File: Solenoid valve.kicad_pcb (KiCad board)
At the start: 2 copper layers, 27.1 x 24.5 mm, 21 parts, among them J2 Conn_01x02, J3 Conn_01x02, J4 Conn_01x02, Q1 S8050, Q2 S8050, U1 BTS443P

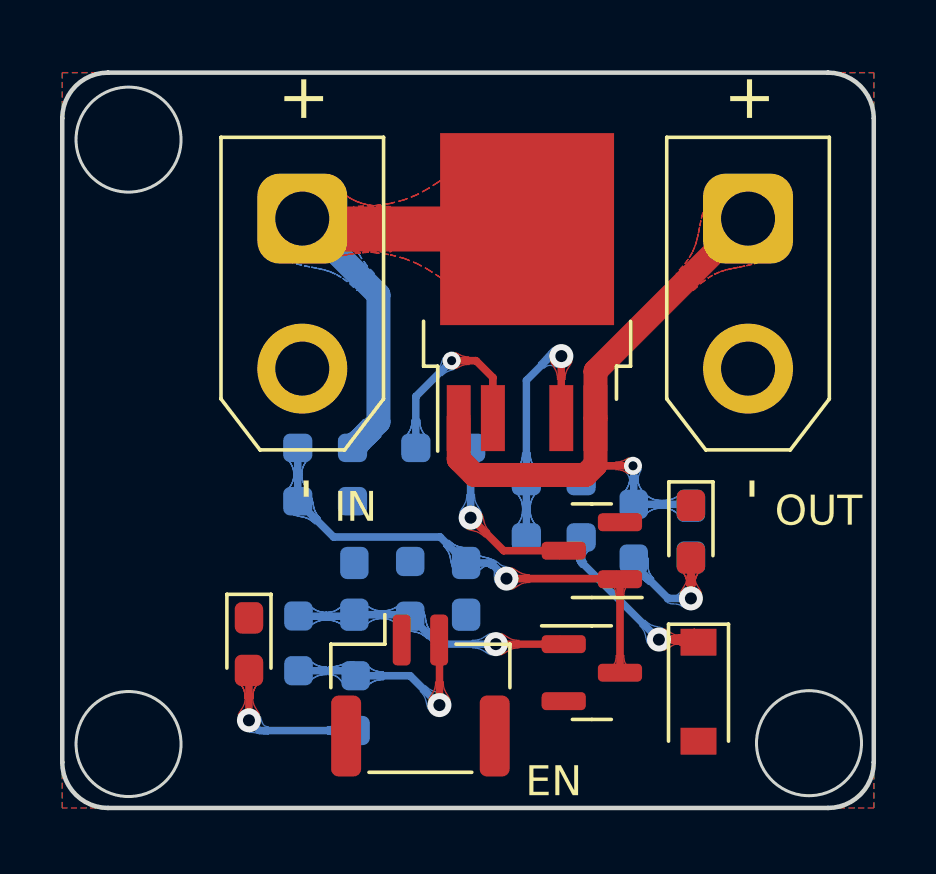
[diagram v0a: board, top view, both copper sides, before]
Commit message: Change somes' positions and add mask
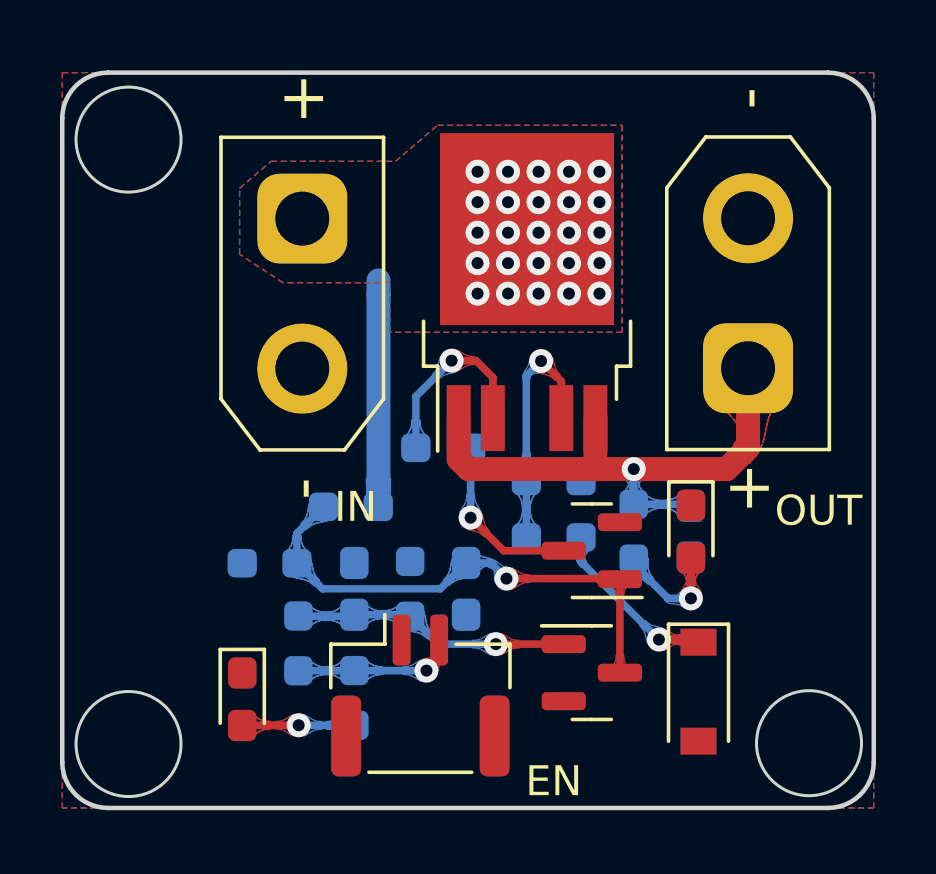
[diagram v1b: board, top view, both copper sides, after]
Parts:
- moved J4 5.01 mm to (128.0, 94.3), turned to -90 degrees
- moved R4 2.78 mm to (112.1, 105.8), turned to 180 degrees
- moved R3 2.15 mm to (114.8, 103.9)
- moved D3 1.85 mm to (111.2, 110.4)
- moved R9 0.18 mm to (114.9, 110.3)
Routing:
- net +24V: track 16.7 -> 8.05 mm, vias 0 -> 25
- net Net-(C3-Pad1): track 21.1 -> 18.9 mm
- net Net-(R1-Pad1): track 7.35 -> 5.43 mm
- net Net-(D3-Pad2): track 5.36 -> 3.75 mm
- net Net-(R6-Pad2): track 8.81 -> 8.26 mm
- added copper zone on B.Cu, net +24V
- added copper zone on F.Cu, net +24V
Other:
- board text added: "10K"
- board text added: "2K"
- board text removed: "DynamicX Solenoid valve_V0 by_LJL"

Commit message: Adjustment for full version
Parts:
- removed C3: 100nF, Capacitor_SMD:C_0603_1608Metric_Pad1.08x0.95mm_HandSolder
- removed D2, D3: LED, LED_SMD:LED_0603_1608Metric_Pad1.05x0.95mm_HandSolder
- removed J4: Conn_01x02, Connector_AMASS:AMASS_XT30UPB-F_1x02_P5.0mm_Vertical
- removed R3: 10k, Resistor_SMD:R_0603_1608Metric_Pad0.98x0.95mm_HandSolder
- added J1: Conn_01x02, Connector_JST:JST_GH_SM02B-GHS-TB_1x02-1MP_P1.25mm_Horizontal, F.Cu at (112.9, 110.5)
- added R10: 9K, Resistor_SMD:R_0603_1608Metric, B.Cu at (121.5, 110.7)
- added R11: 1K, Resistor_SMD:R_0603_1608Metric, F.Cu at (125.4, 104.4)
- added U2: LM5060, Package_SO:VSSOP-10_3x3mm_P0.5mm, B.Cu at (119.2, 105.6)
- C1, C2: value 100nF -> 100n; footprint Capacitor_SMD:C_0603_1608Metric_Pad1.08x0.95mm_HandSolder -> Capacitor_SMD:C_0603_1608Metric
- D1: value D -> LED; footprint Diode_SMD:D_SOD-123 -> Diode_SMD:D_0603_1608Metric
- J2: footprint Connector_JST:JST_GH_SM02B-GHS-TB_1x02-1MP_P1.25mm_Horizontal -> Connector_AMASS:AMASS_XT30UPB-F_1x02_P5.0mm_Vertical
- Q1: value S8050 -> 8050
- Q2: value S8050 -> CSD18540Q5B; footprint Package_TO_SOT_SMD:SOT-23 -> Package_TO_SOT_SMD:TDSON-8-1
- R1: value 100 -> 10K; footprint Resistor_SMD:R_0603_1608Metric_Pad0.98x0.95mm_HandSolder -> Resistor_SMD:R_0603_1608Metric
- R2, R5: value 10k -> 10K; footprint Resistor_SMD:R_0603_1608Metric_Pad0.98x0.95mm_HandSolder -> Resistor_SMD:R_0603_1608Metric
- R4: value 10k -> 47K; footprint Resistor_SMD:R_0603_1608Metric_Pad0.98x0.95mm_HandSolder -> Resistor_SMD:R_0603_1608Metric
- R6: value 10k -> 14K; footprint Resistor_SMD:R_0603_1608Metric_Pad0.98x0.95mm_HandSolder -> Resistor_SMD:R_0603_1608Metric
- R7: value 2k -> 38.3K; footprint Resistor_SMD:R_0603_1608Metric_Pad0.98x0.95mm_HandSolder -> Resistor_SMD:R_0603_1608Metric
- R8: value 10k -> 200K; footprint Resistor_SMD:R_0603_1608Metric_Pad0.98x0.95mm_HandSolder -> Resistor_SMD:R_0603_1608Metric
- R9: value 2k -> 100K; footprint Resistor_SMD:R_0603_1608Metric_Pad0.98x0.95mm_HandSolder -> Resistor_SMD:R_0603_1608Metric
- U1: value BTS443P -> EL357N; footprint Package_TO_SOT_SMD:TO-252-4 -> Package_SO:SOIC-4_4.55x3.7mm_P2.54mm
- moved J2 19.5 mm to (128.3, 94.3), turned to -90 degrees
- moved Q2 12.5 mm to (118.7, 93.6)
- moved R9 11.2 mm to (119.7, 100.3), turned to -90 degrees
- moved U1 10.9 mm to (113.7, 105.1), turned to 0 degrees
- moved R1 9.66 mm to (116.5, 99.5)
- moved R5 9.59 mm to (116.2, 111.4), turned to -90 degrees
- moved R8 9.30 mm to (117.7, 111.4), turned to -90 degrees
- moved R6 8.64 mm to (119.2, 111.4), turned to 90 degrees
- moved C2 6.43 mm to (118.2, 100.3)
- moved D1 6.04 mm to (128.4, 104.4), turned to 180 degrees
- moved Q1 5.98 mm to (120.9, 103.8), turned to 90 degrees
- moved R4 5.13 mm to (113.9, 110.6)
- moved R2 4.19 mm to (116.5, 102.5), turned to -90 degrees
- moved C1 4.18 mm to (114.9, 102.5), turned to -90 degrees
- moved J3 3.80 mm to (109.4, 99.0)
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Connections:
- C1 pad 1: Net-(C1-Pad1) -> GND
- C1 pad 2: Earth -> Net-(C1-Pad2)
- C2 pad 1: Net-(C2-Pad1) -> GND
- C2 pad 2: Earth -> Net-(C2-Pad2)
- D1 pad 1: Net-(D1-Pad1) -> GND
- D1 pad 2: Earth -> Net-(D1-Pad2)
- J2 pad 1: Earth -> Net-(J2-Pad1)
- J2 pad 2: Net-(R1-Pad1) -> GND
- J3 pad 2: Earth -> GND
- Q1 pad 1: Net-(C1-Pad1) -> Net-(C1-Pad2)
- Q1 pad 2: Earth -> GND
- Q1 pad 3: Net-(C2-Pad1) -> Net-(Q1-Pad3)
- Q2 pad 1: Net-(C2-Pad1) -> Net-(J2-Pad1)
- Q2 pad 2: Earth -> Net-(J2-Pad1)
- Q2 pad 3: Net-(Q2-Pad3) -> Net-(J2-Pad1)
- R1 pad 2: Net-(C1-Pad1) -> +24V
- R2 pad 1: Net-(C1-Pad1) -> Net-(R1-Pad1)
- R2 pad 2: Earth -> Net-(C1-Pad2)
- R4 pad 1: Net-(C2-Pad1) -> Net-(Q1-Pad3)
- R4 pad 2: Earth -> +24V
- R5 pad 1: Net-(Q2-Pad3) -> Net-(Q1-Pad3)
- R5 pad 2: Net-(R5-Pad2) -> GND
- R6 pad 1: Earth -> GND
- R7 pad 1: Net-(R6-Pad2) -> Net-(R7-Pad1)
- R7 pad 2: Net-(D1-Pad1) -> Net-(R6-Pad2)
- R8 pad 1: Net-(D2-Pad2) -> Net-(R7-Pad1)
- R8 pad 2: Net-(C3-Pad1) -> +24V
- R9 pad 1: Net-(D3-Pad2) -> +24V
- R9 pad 2: Net-(R1-Pad1) -> Net-(R9-Pad2)
- U1 pad 1: Net-(C3-Pad1) -> Net-(J1-Pad2)
- U1 pad 2: Net-(R5-Pad2) -> Net-(J1-Pad1)
- U1 pad 3: +24V -> GND
- U1 pad 4: Net-(R6-Pad2) -> Net-(R1-Pad1)
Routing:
- net +24V: track 8.05 -> 32.8 mm, vias 25 -> 22
- net Net-(C3-Pad1): track 18.9 -> 0.00 mm, vias 1 -> 0
- net Net-(C2-Pad1): track 17.1 -> 0.00 mm, vias 1 -> 0
- net Net-(J2-Pad1): track 0.00 -> 14.8 mm, vias 0 -> 7
- net Net-(Q2-Pad4): track 0.00 -> 13.3 mm, vias 0 -> 1
- net Net-(Q1-Pad3): track 0.00 -> 12.0 mm, vias 0 -> 1
- net Net-(C1-Pad1): track 9.34 -> 0.00 mm, vias 1 -> 0
- net Net-(R7-Pad1): track 0.00 -> 8.29 mm
- net Net-(J1-Pad2): track 0.00 -> 7.37 mm
- net Net-(R5-Pad2): track 6.36 -> 0.00 mm, vias 1 -> 0
- net Net-(Q2-Pad3): track 5.89 -> 0.00 mm, vias 1 -> 0
- net Net-(D1-Pad1): track 5.83 -> 0.00 mm, vias 1 -> 0
- net Net-(C1-Pad2): track 0.00 -> 5.56 mm, vias 0 -> 1
- net Net-(J1-Pad1): track 0.00 -> 3.94 mm
- net Net-(D2-Pad2): track 3.90 -> 0.00 mm, vias 1 -> 0
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- added copper zone on B.Cu, net GND
- added copper zone on F.Cu, net GND
- added copper zone on B.Cu, net Net-(J2-Pad1)
- added copper zone on F.Cu, net Net-(J2-Pad1)
- removed copper zone on B.Cu, net Earth
- removed copper zone on F.Cu, net Earth
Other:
- outline, holes or cut-outs redrawn
- board text added: "100K"
- board text added: "14K"
- board text added: "1K"
- board text added: "200K"
- board text added: "38.3K"
- board text added: "47K"
- board text added: "9K"
- board text removed: "2K"

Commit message: Add protectionfor EN
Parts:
- added H1: MountingHole, MountingHole:MountingHole_2.7mm_M2.5, F.Cu at (107.4, 111.8)
- added H2: MountingHole, MountingHole:MountingHole_2.7mm_M2.5, F.Cu at (130.0, 111.8)
- added R12: 1K, Resistor_SMD:R_0603_1608Metric, B.Cu at (113.1, 105.9)
- turned C1 to 90 degrees
- turned C2 to 90 degrees
- turned R2 to 90 degrees
- turned R5 to 90 degrees
- turned R9 to 90 degrees
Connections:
- C1 pad 1: GND -> Net-(C1-Pad1)
- C1 pad 2: Net-(C1-Pad2) -> GND
- C2 pad 1: GND -> Net-(C2-Pad1)
- C2 pad 2: Net-(C2-Pad2) -> GND
- Q1 pad 1: Net-(C1-Pad2) -> Net-(C1-Pad1)
- R2 pad 1: Net-(R1-Pad1) -> Net-(C1-Pad1)
- R2 pad 2: Net-(C1-Pad2) -> Net-(R1-Pad1)
- R5 pad 1: Net-(Q1-Pad3) -> GND
- R5 pad 2: GND -> Net-(Q1-Pad3)
- R9 pad 1: +24V -> Net-(R9-Pad1)
- R9 pad 2: Net-(R9-Pad2) -> +24V
- U1 pad 1: Net-(J1-Pad2) -> Net-(R12-Pad1)
- U2 pad 7: Net-(C2-Pad2) -> Net-(C2-Pad1)
- U2 pad 8: Net-(R9-Pad2) -> Net-(R9-Pad1)
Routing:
- net Net-(C1-Pad2): track 5.56 -> 0.00 mm, vias 1 -> 0
- net Net-(C1-Pad1): track 0.00 -> 5.56 mm, vias 0 -> 1
- net Net-(J1-Pad2): track 7.37 -> 2.96 mm, vias 0 -> 1
- net Net-(R12-Pad1): track 0.00 -> 3.40 mm, vias 0 -> 1
- net Net-(C2-Pad2): track 2.57 -> 0.00 mm
- net Net-(C2-Pad1): track 0.00 -> 2.57 mm
- net Net-(R9-Pad2): track 2.52 -> 0.00 mm
- net Net-(R9-Pad1): track 0.00 -> 2.52 mm

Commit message: Add protection for OUT
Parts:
- added D2: SS34A, Diode_SMD:D_SMA, B.Cu at (123.4, 95.3)
- D1: footprint Diode_SMD:D_0603_1608Metric -> LED_SMD:LED_0603_1608Metric
- moved J2 3.78 mm to (128.3, 98.1), turned to 90 degrees
- moved U1 1.78 mm to (112.8, 103.6)
- moved J3 1.10 mm to (109.4, 97.9)
- moved Q2 1.10 mm to (118.7, 92.5)
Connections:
- J2 pad 1: Net-(J2-Pad1) -> GND
- J2 pad 2: GND -> Net-(D2-Pad1)
- Q2 pad 1: Net-(J2-Pad1) -> Net-(D2-Pad2)
- Q2 pad 2: Net-(J2-Pad1) -> Net-(D2-Pad2)
- Q2 pad 3: Net-(J2-Pad1) -> Net-(D2-Pad2)
- R11 pad 2: Net-(J2-Pad1) -> Net-(D2-Pad2)
- U2 pad 9: Net-(J2-Pad1) -> Net-(D2-Pad2)
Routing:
- net Net-(J2-Pad1): track 14.8 -> 0.00 mm, vias 7 -> 0
- net Net-(D2-Pad2): track 0.00 -> 12.9 mm, vias 0 -> 6
- net Net-(R12-Pad1): track 3.40 -> 5.03 mm
- net +24V: track 32.8 -> 34.1 mm
- net Net-(J1-Pad1): track 3.94 -> 5.30 mm
- net Net-(Q2-Pad4): track 13.3 -> 14.0 mm
- added copper zone on B.Cu, net Net-(D2-Pad1)
- added copper zone on F.Cu, net Net-(D2-Pad1)
- added copper zone on B.Cu, net Net-(D2-Pad2)
- added copper zone on F.Cu, net Net-(D2-Pad2)
- removed copper zone on B.Cu, net Net-(J2-Pad1)
- removed copper zone on F.Cu, net Net-(J2-Pad1)

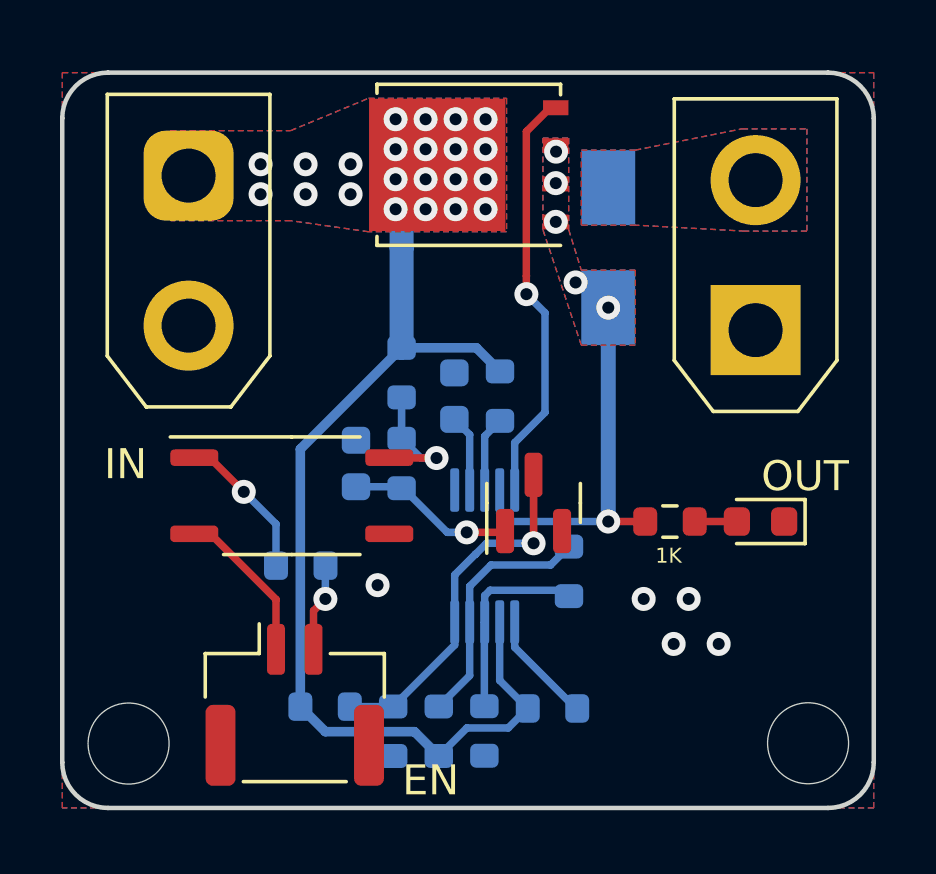
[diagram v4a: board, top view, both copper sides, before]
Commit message: Add teardrops
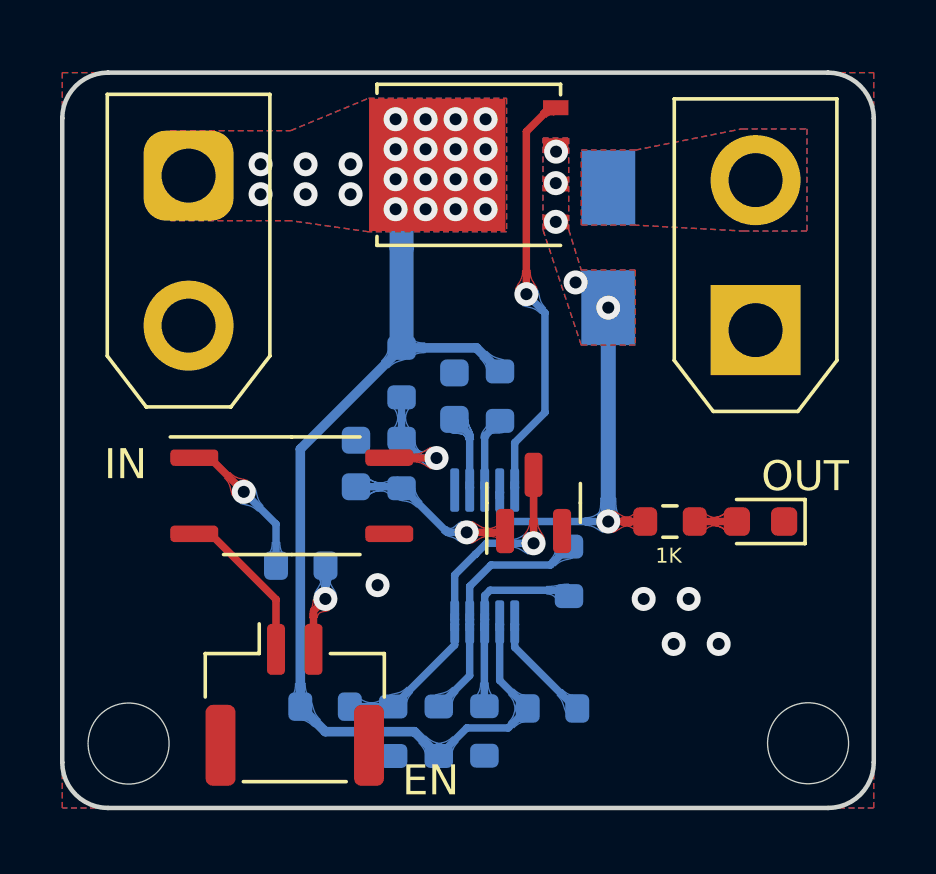
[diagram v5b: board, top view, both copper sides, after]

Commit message: Add a mimic ss34a on the top
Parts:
- added D3: SS34A, Diode_SMD:D_SMA, F.Cu at (123.4, 95.3)

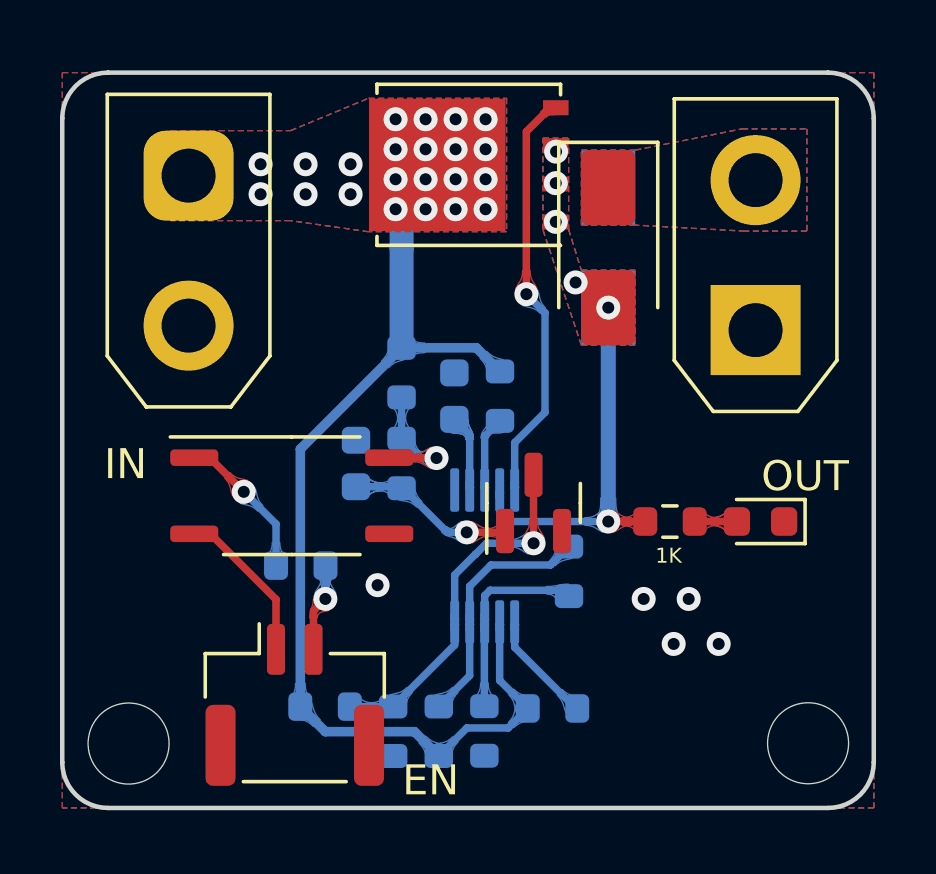
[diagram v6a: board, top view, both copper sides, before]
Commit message: Add a 24V voltage regulator diode
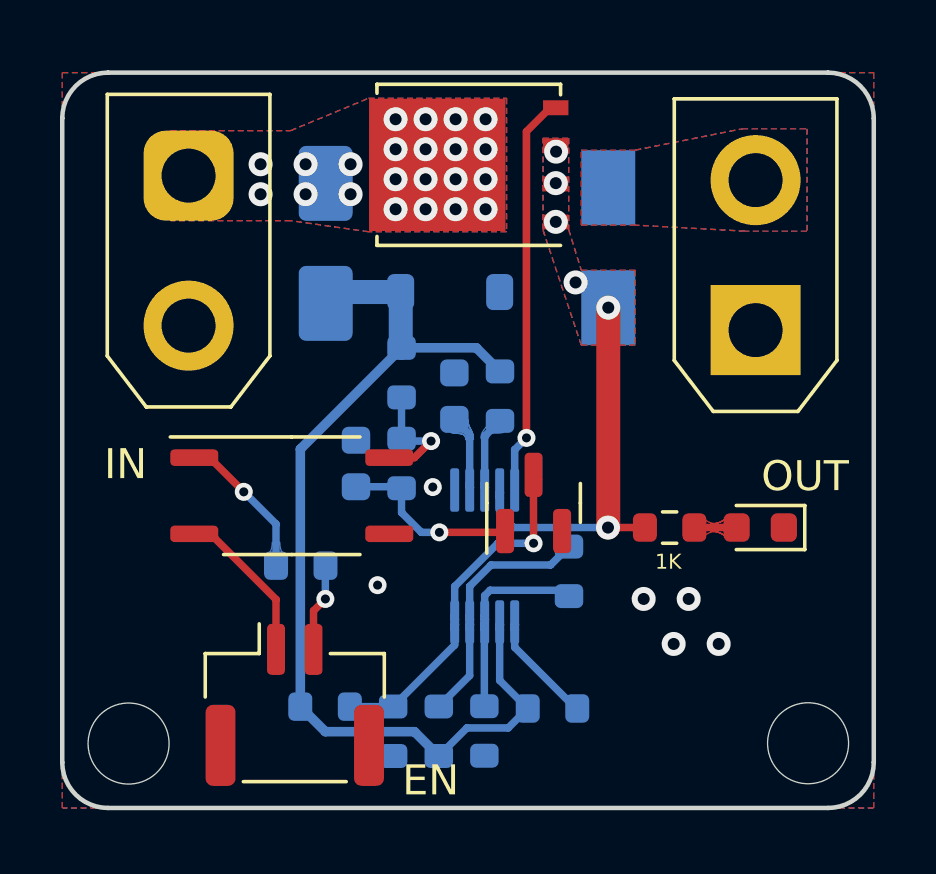
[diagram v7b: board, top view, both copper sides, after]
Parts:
- added D4: 24V, Diode_SMD:D_SOD-123, B.Cu at (118.1, 96.8)
- D3: moved to B.Cu
- moved D3 9.42 mm to (113.9, 95.2), turned to 90 degrees
- moved R11 0.20 mm to (125.4, 104.6)
- moved D1 0.20 mm to (128.4, 104.6)
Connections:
- D3 pad 1: Net-(D2-K) -> Net-(D3-K)
- D3 pad 2: Net-(D2-A) -> +24V
- R1 pad 2: +24V -> Net-(D3-K)
- R10 pad 1: +24V -> Net-(D3-K)
- R4 pad 2: +24V -> Net-(D3-K)
- R8 pad 2: +24V -> Net-(D3-K)
- R9 pad 2: +24V -> Net-(D3-K)
- U2 pad 2: +24V -> Net-(D3-K)
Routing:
- net +24V: track 33.9 -> 0.00 mm
- net Net-(D3-K): track 0.00 -> 33.7 mm
- net Net-(Q2-G): track 14.0 -> 13.5 mm
- net GND: vias 5 -> 6

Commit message: Delete the input_diode
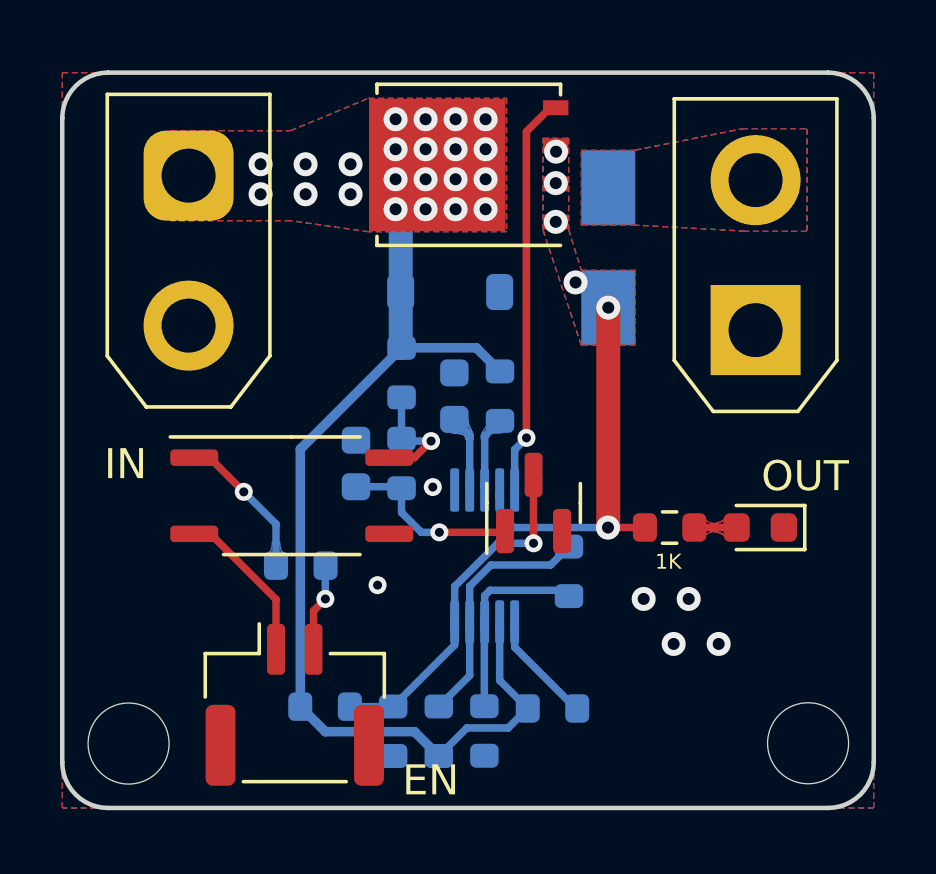
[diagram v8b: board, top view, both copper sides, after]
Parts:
- removed D3: SS34A, Diode_SMD:D_SMA
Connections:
- D4 pad 1: Net-(D3-K) -> +24V
- R1 pad 2: Net-(D3-K) -> +24V
- R10 pad 1: Net-(D3-K) -> +24V
- R4 pad 2: Net-(D3-K) -> +24V
- R8 pad 2: Net-(D3-K) -> +24V
- R9 pad 2: Net-(D3-K) -> +24V
- U2 pad 2: Net-(D3-K) -> +24V
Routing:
- net +24V: track 0.00 -> 33.9 mm
- net Net-(D3-K): track 33.7 -> 0.00 mm
